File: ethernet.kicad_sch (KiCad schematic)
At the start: 51 parts, among them J1 L834-1G1T-S7, U1 KSZ9031RNXCA, U22 ASEMB-25.000MHZ-LC-T

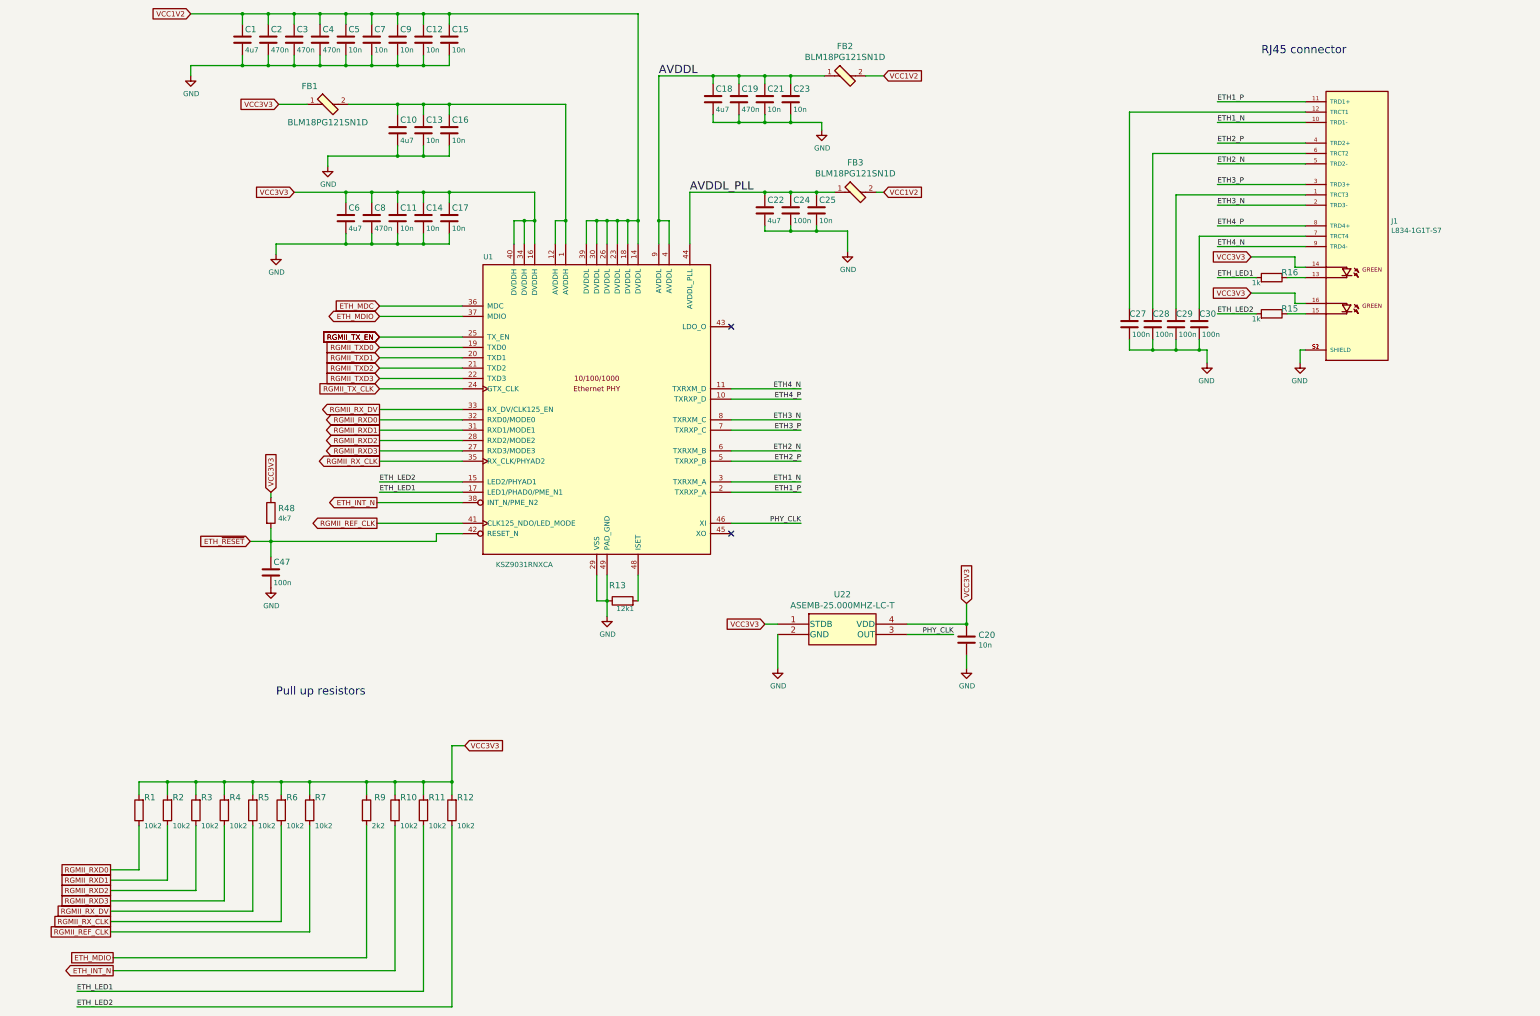
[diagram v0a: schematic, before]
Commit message: [#61392] Convert project to KiCad 7
[#61392] Run globlib

[#61392] Allign components to the grid

[#61392] Update oshw and antmicro logo

[#61392] Standarize ethernet sheet

[#61392] Standarize pcie-conn sheet

[#61392] Standarize rot sheet

[#61392] Standarize edge-connector sheet

[#61392] WIP:Standarize interfaces sheet

[#61392] WIP: Route interfaces sheet

[#61392] Finish standarizing interfaces sheet

[#61392] Update interfaces sheet with fixed 2N7002

[#61392] WIP:Standarize ddr3 sheet

[#61392] Standarize ddr3 sheet

[#61392] Standarize power-supply sheet

[#61392] Standarize fpga power-supply sheet

[#61392] Remove TODO comments from power-banks sheet

[#61392] Standarize fpga-banks sheet

[#61392] Ignore Input pins not driven ERC

[#61392] Clear off grid ERCs

[#61392] Exclude ERC DDR3_VTT_EN NC

[#61392] Bump rev to 1.2.1

[#61392] Bump PCB rev to 1.2.1
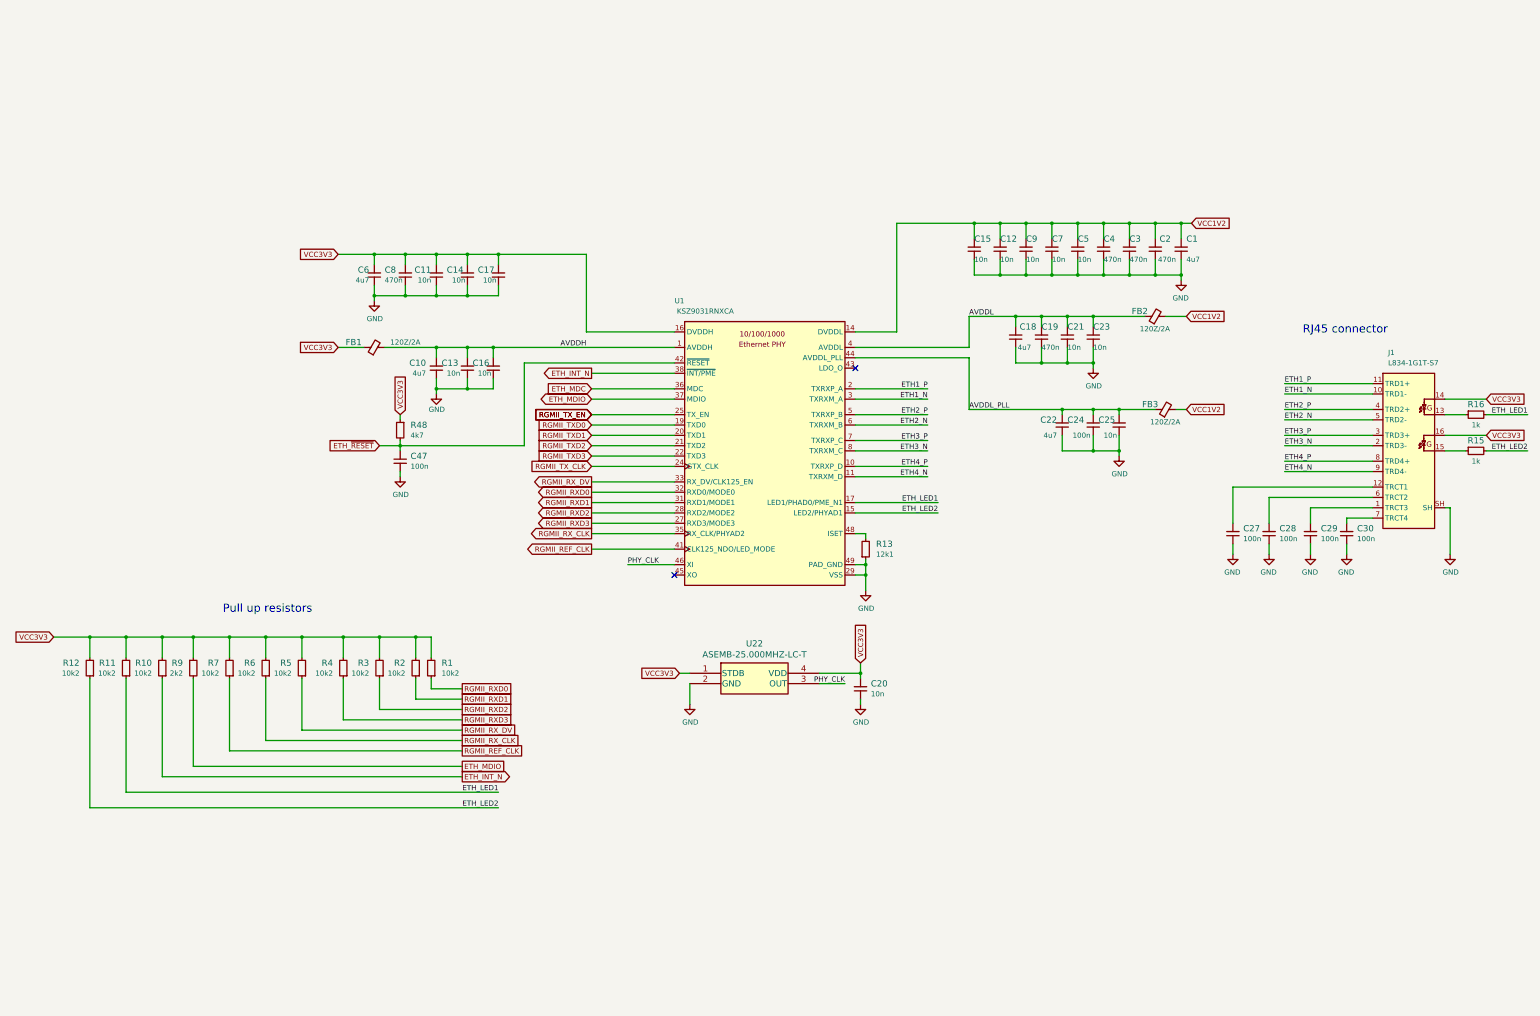
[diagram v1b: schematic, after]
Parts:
- C1, C10, C18, C22, C6: footprint ecp5-dc-scm-footprints:0402-cap -> antmicro-footprints:C_0402_1005Metric; symbol ecp5-dc-scm:C_4u7_0402 -> antmicroCapacitors0402:C_4u7_0402; Author (none) -> Antmicro; License (none) -> Apache-2.0; Manufacturer MURATA -> Murata; Public (none) -> False
- C11, C12, C13, C14, C15, C16, C17, C20, C21, C23, C25, C5, C7, C9: footprint ecp5-dc-scm-footprints:0402-cap -> antmicro-footprints:C_0402_1005Metric; symbol ecp5-dc-scm:C_10n_0402 -> antmicroCapacitors0402:C_10n_0402; Author (none) -> Antmicro; Dielectric (none) -> X7R; License (none) -> Apache-2.0; MPN 04025G103ZAT2A -> GRM155R71H103KA88D; Manufacturer AVX -> Murata; Public (none) -> False; Voltage (none) -> 50V
- C19, C2, C3, C4, C8: footprint ecp5-dc-scm-footprints:0402-cap -> antmicro-footprints:C_0402_1005Metric; symbol ecp5-dc-scm:C_470n_0402 -> antmicroCapacitors0402:C_470n_0402; Author (none) -> Antmicro; License (none) -> Apache-2.0; Public (none) -> False
- C24, C27, C28, C29, C30, C47: footprint ecp5-dc-scm-footprints:0402-cap -> antmicro-footprints:C_0402_1005Metric; symbol ecp5-dc-scm:C_100n_0402 -> antmicroCapacitors0402:C_100n_0402; Author (none) -> Antmicro; Dielectric (none) -> X5R; License (none) -> Apache-2.0; MPN 0402X104K6R3CT -> GRM155R61H104KE14D; Manufacturer Walsin -> Murata; Public (none) -> False; Voltage (none) -> 50V
- FB1, FB2, FB3: value BLM18PG121SN1D -> FB_120Z_2A_Murata-BLM18PG_0603; footprint ecp5-dc-scm-footprints:0603-res -> antmicro-footprints:FB_0603_1608Metric; symbol ecp5-dc-scm:BLM18PG121SN1D -> antmicroFerriteBeadsandChips:FB_120Z_2A_Murata-BLM18PG_0603; Author (none) -> Antmicro; License (none) -> Apache-2.0; Manufacturer Murata Electronics North America -> Murata; Public (none) -> False; Val (none) -> 120Z/2A
- J1: footprint ecp5-dc-scm-footprints:BEL_L834-1G1T-S7 -> antmicro-footprints:RJ45_BEL_L834-1G1T-S7; symbol ecp5-dc-scm:L834-1G1T-S7 -> antmicroModularConnectorsJacksWithMagnetics:L834-1G1T-S7; Author (none) -> Antmicro; License (none) -> Apache-2.0; Manufacturer Bel Magnetic Solutions -> Bel Fuse
- R1, R10, R11, R12, R2, R3, R4, R5, R6, R7: footprint ecp5-dc-scm-footprints:0402-res -> antmicro-footprints:R_0402_1005Metric; symbol ecp5-dc-scm:R_10k2_0402 -> antmicroResistors0402:R_10k2_0402; Author (none) -> Antmicro; License (none) -> Apache-2.0; MPN MCWR04X1022FTL -> CR0402-FX-1022GLF; Manufacturer MULTICOMP PRO -> Bourns; Public (none) -> False; Tolerance (none) -> 1%
- R13: footprint ecp5-dc-scm-footprints:0402-res -> antmicro-footprints:R_0402_1005Metric; symbol ecp5-dc-scm:R_12k1_0402 -> antmicroResistors0402:R_12k1_0402; Author (none) -> Antmicro; License (none) -> Apache-2.0; MPN MCWR04X1212FTL -> CR0402-FX-1212GLF; Manufacturer MULTICOMP -> Bourns; Public (none) -> False; Tolerance (none) -> 1%
- R15, R16: footprint ecp5-dc-scm-footprints:0402-res -> antmicro-footprints:R_0402_1005Metric; symbol ecp5-dc-scm:R_1k_0402 -> antmicroResistors0402:R_1k_0402; Author (none) -> Antmicro; License (none) -> Apache-2.0; Manufacturer BOURNS -> Bourns; Public (none) -> False; Tolerance (none) -> 1%
- R48: footprint ecp5-dc-scm-footprints:0402-res -> antmicro-footprints:R_0402_1005Metric; symbol ecp5-dc-scm:R_4k7_0402 -> antmicroResistors0402:R_4k7_0402; Author (none) -> Antmicro; License (none) -> Apache-2.0; MPN ERJ2GEJ472X -> CR0402-FX-4701GLF; Manufacturer PANASONIC_ELECTRONIC_COMPONENTS -> Bourns; Public (none) -> False; Tolerance (none) -> 1%
- R9: footprint ecp5-dc-scm-footprints:0402-res -> antmicro-footprints:R_0402_1005Metric; symbol ecp5-dc-scm:R_2k2_0402 -> antmicroResistors0402:R_2k2_0402; Author (none) -> Antmicro; License (none) -> Apache-2.0; MPN RC0402FR-072K2L -> CR0402-FX-2201GLF; Manufacturer YAGEO -> Bourns; Public (none) -> False; Tolerance (none) -> 1%
- U1: footprint ecp5-dc-scm-footprints:QFN-48-Microchip-QFN77-48LD-PL-2 -> antmicro-footprints:QFN-48-1EP_7x7x0.9mm_P0.5mm_EP3.5x3.5mm; symbol ecp5-dc-scm:KSZ9031RNXCA -> antmicroInterfaceControllers:KSZ9031RNXCA; Author (none) -> Antmicro; License (none) -> Apache-2.0; Manufacturer Microchip -> Microchip Technology
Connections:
- net AVDDL: now also C18.2, C19.2, C21.2, C23.2; no longer C18.1, C19.1, C21.1, C23.1
- net AVDDL_PLL: now also C22.2, C24.2, C25.2; no longer C22.1, C24.1, C25.1
- net GND: now also C1.1, C10.1, C11.1, C12.1, C13.1, C14.1, C15.1, C16.1, C17.1, C18.1, C19.1, C2.1, C20.1, C21.1, C22.1, C23.1, C24.1, C25.1, C27.1, C28.1, C29.1, C3.1, C30.1, C4.1, C5.1, C6.1, C7.1, C8.1, C9.1, J1.SH; no longer C1.2, C10.2, C11.2, C12.2, C13.2, C14.2, C15.2, C16.2, C17.2, C18.2, C19.2, C2.2, C20.2, C21.2, C22.2, C23.2, C24.2, C25.2, C27.2, C28.2, C29.2, C3.2, C30.2, C4.2, C5.2, C6.2, C7.2, C8.2, C9.2, J1.S1 (SHIELD), J1.S2 (SHIELD)
- net VCC1V2: now also C1.2, C12.2, C15.2, C2.2, C3.2, C4.2, C5.2, C7.2, C9.2; no longer C1.1, C12.1, C15.1, C2.1, C3.1, C4.1, C5.1, C7.1, C9.1
- net VCC3V3: now also C11.2, C14.2, C17.2, C20.2, C6.2, C8.2; no longer C11.1, C14.1, C17.1, C20.1, C6.1, C8.1
- net AVDDH: now reaches FB1.2, U1.1 (AVDDH), U1.12 (AVDDH)
- net AVDDH: now also C10.2, C13.2, C16.2; no longer C10.1, C13.1, C16.1
- net at J1.7 (TRCT4): now also C30.2; no longer C30.1
- net at J1.1 (TRCT3): now also C29.2; no longer C29.1
- net at J1.6 (TRCT2): now also C28.2; no longer C28.1
- net at J1.12 (TRCT1): now also C27.2; no longer C27.1
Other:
- moved on the sheet: C1, C10, C11, C12, C13, C14, C15, C16, C17, C18, C19, C2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

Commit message: [#61392] Import changes to the PCB
[#61392] Fix D2 orientation

[#61392] Fix J2 J1 D6 orientation

[#61392] WIP: PCB Fix caps orienations

[#61392] PCB Fix caps orienations

[#61392] Fix missalligned edge cuts

[#61392] Sync Sch with PCB

[#61392] Fix silk clipped by edge cuts

[#61392] Ignore TP no courtyard drc

[#61392] Update C_0603 footprints

[#61392] Update R_0402 footprints

[#61392] Update Sot-23 footprints

[#61392] Update QFN and IHLP footprints

[#61392] Update remaining footprints

[#61392] Change minimal text height to 0.7mm

[#61392] Clear remaining Silk DRCs

[#61392] Update TPS51200DRCT symbol

[#61392] Update 9774040151

[#61392] Update W25Q32JVS

[#61392] Update ECS-3225MVQ-1000CN-TR

[#61392] Clean ERC

[#61392] Remove obsolete files

[#61392] Synhronize components with library

[#61392] Remove globlib leftovers

[#61392] Synchronize components with libraries (WiP)

[#61392] Clean ERC and DRC

[#61392] Set J5 to DNP

[#61392] Add PCB SHA string, update layer names

[#61392] Update assets

[#62567] Add stackup.csv

[#62567] Input elecric constants for the board stackup

[#62567] Update stackup.csv
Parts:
- removed U22: ASEMB-25.000MHZ-LC-T, ecp5-dc-scm-footprints:OSC_ASEM1-16.000MHZ-LC-T, symbol ecp5-dc-scm:ASEMB-25.000MHZ-LC-T
- added Y5: Oscillator_25MHz_ESC_2016MV, antmicro-footprints:Oscillator_SMD_ECS_2016MV_2x1.6x0.85mm, symbol antmicroOscillators:Oscillator_25MHz_ESC_2016MV
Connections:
- net GND: now also Y5.2 (GND)
- net PHY_CLK: now also Y5.3 (OUT)
- net VCC3V3: now also Y5.1 (EN), Y5.4 (VDD)
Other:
- moved on the sheet: C20
